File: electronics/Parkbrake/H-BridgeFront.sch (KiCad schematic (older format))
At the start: 74 parts, among them Q19 NX3008CBKS, Q20 IPD031N06L3 G, Q21 IPD031N06L3 G, Q22 IPD031N06L3 G, Q23 IPD031N06L3 G, Q24 NX3008CBKS, Q25 NX3008CBKS, Q26 IPD031N06L3 G, Q27 IPD031N06L3 G, Q28 IPD031N06L3 G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

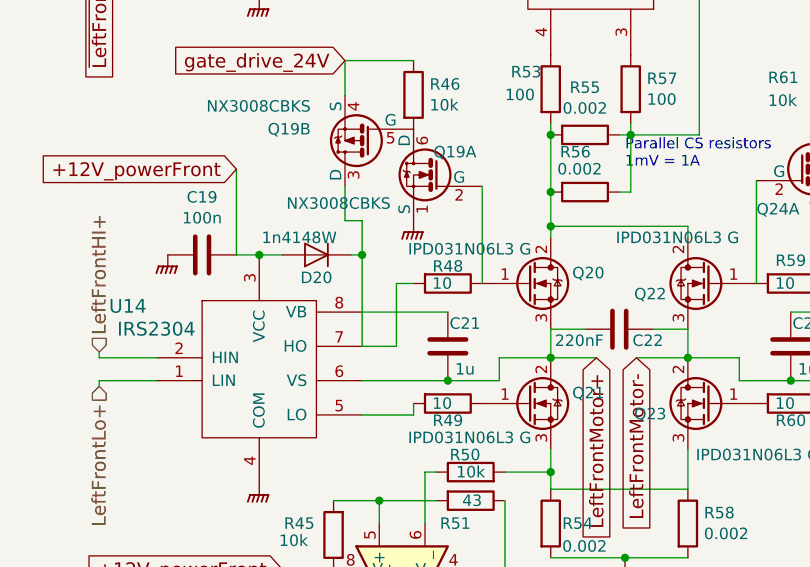
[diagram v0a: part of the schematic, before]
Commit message: Front motors H-bridge finished
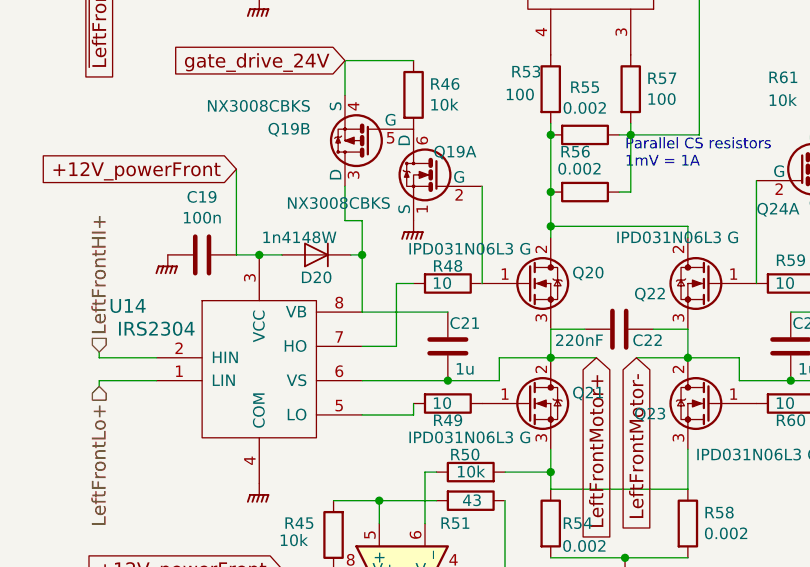
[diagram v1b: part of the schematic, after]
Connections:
- net at D20.1 (K), Q19.3 (D): now also C21.2, U14.8 (VB); no longer R48.2, U14.7 (HO)
- new net: R48.2, U14.7 (HO)
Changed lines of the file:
@@
 $EndComp
 $Comp
-L GNDPWR #PWR42
+L GNDPWR #PWR044
 U 1 1 57012736
 P 3175 4850
-F 0 "#PWR42" H 3175 4650 50  0001 C CNN
+F 0 "#PWR044" H 3175 4650 50  0001 C CNN
 F 1 "GNDPWR" H 3182 4924 50  0001 C CNN
 F 2 "" H 3175 4800 50  0000 C CNN
@@
 $EndComp
 $Comp
-L GNDPWR #PWR46
+L GNDPWR #PWR045
 U 1 1 5797A569
 P 5075 3525
-F 0 "#PWR46" H 5075 3325 50  0001 C CNN
+F 0 "#PWR045" H 5075 3325 50  0001 C CNN
 F 1 "GNDPWR" H 5082 3599 50  0001 C CNN
 F 2 "" H 5075 3475 50  0000 C CNN
@@
 $EndComp
 $Comp
-L GNDPWR #PWR45
+L GNDPWR #PWR046
 U 1 1 57018D81
 P 4675 4525
-F 0 "#PWR45" H 4675 4325 50  0001 C CNN
+F 0 "#PWR046" H 4675 4325 50  0001 C CNN
 F 1 "GNDPWR" H 4682 4599 50  0001 C CNN
 F 2 "" H 4675 4475 50  0000 C CNN
@@
 $EndComp
 $Comp
-L GNDPWR #PWR37
+L GNDPWR #PWR047
 U 1 1 5701B14E
 P 1575 4525
-F 0 "#PWR37" H 1575 4325 50  0001 C CNN
+F 0 "#PWR047" H 1575 4325 50  0001 C CNN
 F 1 "GNDPWR" H 1582 4599 50  0001 C CNN
 F 2 "" H 1575 4475 50  0000 C CNN
@@
 $EndComp
 $Comp
-L GNDPWR #PWR35
+L GNDPWR #PWR048
 U 1 1 5701CA40
 P 1175 3525
-F 0 "#PWR35" H 1175 3325 50  0001 C CNN
+F 0 "#PWR048" H 1175 3325 50  0001 C CNN
 F 1 "GNDPWR" H 1182 3599 50  0001 C CNN
 F 2 "" H 1175 3475 50  0000 C CNN
@@
 $EndComp
 $Comp
-L GNDPWR #PWR38
+L GNDPWR #PWR049
 U 1 1 5701EEBF
 P 1900 5200
-F 0 "#PWR38" H 1900 5000 50  0001 C CNN
+F 0 "#PWR049" H 1900 5000 50  0001 C CNN
 F 1 "GNDPWR" H 1907 5274 50  0001 C CNN
 F 2 "" H 1900 5150 50  0000 C CNN
@@
 $EndComp
 $Comp
-L GNDPWR #PWR41
+L GNDPWR #PWR050
 U 1 1 5701EFC1
 P 2650 4900
-F 0 "#PWR41" H 2650 4700 50  0001 C CNN
+F 0 "#PWR050" H 2650 4700 50  0001 C CNN
 F 1 "GNDPWR" H 2657 4974 50  0001 C CNN
 F 2 "" H 2650 4850 50  0000 C CNN
@@
 $EndComp
 $Comp
-L GNDPWR #PWR54
+L GNDPWR #PWR051
 U 1 1 57031398
 P 8300 4825
-F 0 "#PWR54" H 8300 4625 50  0001 C CNN
+F 0 "#PWR051" H 8300 4625 50  0001 C CNN
 F 1 "GNDPWR" H 8307 4899 50  0001 C CNN
 F 2 "" H 8300 4775 50  0000 C CNN
@@
 $EndComp
 $Comp
-L GNDPWR #PWR58
+L GNDPWR #PWR052
 U 1 1 57031429
 P 10200 3500
-F 0 "#PWR58" H 10200 3300 50  0001 C CNN
+F 0 "#PWR052" H 10200 3300 50  0001 C CNN
 F 1 "GNDPWR" H 10207 3574 50  0001 C CNN
 F 2 "" H 10200 3450 50  0000 C CNN
@@
 $EndComp
 $Comp
-L GNDPWR #PWR57
+L GNDPWR #PWR053
 U 1 1 5703142F
 P 9800 4500
-F 0 "#PWR57" H 9800 4300 50  0001 C CNN
+F 0 "#PWR053" H 9800 4300 50  0001 C CNN
 F 1 "GNDPWR" H 9807 4574 50  0001 C CNN
 F 2 "" H 9800 4450 50  0000 C CNN
@@
 $EndComp
 $Comp
-L GNDPWR #PWR49
+L GNDPWR #PWR054
 U 1 1 5797A59B
 P 6700 4500
-F 0 "#PWR49" H 6700 4300 50  0001 C CNN
+F 0 "#PWR054" H 6700 4300 50  0001 C CNN
 F 1 "GNDPWR" H 6707 4574 50  0001 C CNN
 F 2 "" H 6700 4450 50  0000 C CNN
@@
 $EndComp
 $Comp
-L GNDPWR #PWR47
+L GNDPWR #PWR055
 U 1 1 57031456
 P 6300 3500
-F 0 "#PWR47" H 6300 3300 50  0001 C CNN
+F 0 "#PWR055" H 6300 3300 50  0001 C CNN
 F 1 "GNDPWR" H 6307 3574 50  0001 C CNN
 F 2 "" H 6300 3450 50  0000 C CNN
@@
 $EndComp
 $Comp
-L GNDPWR #PWR50
+L GNDPWR #PWR056
 U 1 1 5703147D
 P 7025 5175
-F 0 "#PWR50" H 7025 4975 50  0001 C CNN
+F 0 "#PWR056" H 7025 4975 50  0001 C CNN
 F 1 "GNDPWR" H 7032 5249 50  0001 C CNN
 F 2 "" H 7025 5125 50  0000 C CNN
@@
 $EndComp
 $Comp
-L GNDPWR #PWR53
+L GNDPWR #PWR057
 U 1 1 5797A5A5
 P 7775 4875
-F 0 "#PWR53" H 7775 4675 50  0001 C CNN
+F 0 "#PWR057" H 7775 4675 50  0001 C CNN
 F 1 "GNDPWR" H 7782 4949 50  0001 C CNN
 F 2 "" H 7775 4825 50  0000 C CNN
@@
 Connection ~ 2400 4075
 Wire Wire Line
-	2400 3775 2025 3775
+	2025 3775 2400 3775
 Wire Wire Line
 	2250 4175 2250 4225
 Wire Wire Line
 	2250 4225 2025 4225
-Wire Wire Line
-	2025 3375 2025 3925
 Wire Wire Line
 	2250 3650 2175 3650
@@
 	1950 2675 1950 2825
 $Comp
-L GNDPWR #PWR44
+L GNDPWR #PWR058
 U 1 1 5797A5B1
 P 4050 3350
-F 0 "#PWR44" H 4050 3150 50  0001 C CNN
+F 0 "#PWR058" H 4050 3150 50  0001 C CNN
 F 1 "GNDPWR" H 4057 3424 50  0001 C CNN
 F 2 "" H 4050 3300 50  0000 C CNN
@@
 $EndComp
 $Comp
-L GNDPWR #PWR39
+L GNDPWR #PWR059
 U 1 1 5704214E
 P 2250 3375
-F 0 "#PWR39" H 2250 3175 50  0001 C CNN
+F 0 "#PWR059" H 2250 3175 50  0001 C CNN
 F 1 "GNDPWR" H 2257 3449 50  0001 C CNN
 F 2 "" H 2250 3325 50  0000 C CNN
@@
 $EndComp
 $Comp
-L GNDPWR #PWR56
+L GNDPWR #PWR060
 U 1 1 5797A5B3
 P 9175 3350
-F 0 "#PWR56" H 9175 3150 50  0001 C CNN
+F 0 "#PWR060" H 9175 3150 50  0001 C CNN
 F 1 "GNDPWR" H 9182 3424 50  0001 C CNN
 F 2 "" H 9175 3300 50  0000 C CNN
@@
 	7675 3625 7675 3200
 $Comp
-L GNDPWR #PWR51
+L GNDPWR #PWR061
 U 1 1 5797A5B6
 P 7375 3350
-F 0 "#PWR51" H 7375 3150 50  0001 C CNN
+F 0 "#PWR061" H 7375 3150 50  0001 C CNN
 F 1 "GNDPWR" H 7382 3424 50  0001 C CNN
 F 2 "" H 7375 3300 50  0000 C CNN
@@
 	7075 2650 7075 2800
 $Comp
-L GNDPWR #PWR36
+L GNDPWR #PWR062
 U 1 1 5797A5B8
 P 1575 2400
-F 0 "#PWR36" H 1575 2200 50  0001 C CNN
+F 0 "#PWR062" H 1575 2200 50  0001 C CNN
 F 1 "GNDPWR" H 1582 2474 50  0001 C CNN
 F 2 "" H 1575 2350 50  0000 C CNN
@@
 $EndComp
 $Comp
-L GNDPWR #PWR48
+L GNDPWR #PWR063
 U 1 1 5797A5B9
 P 6700 2375
-F 0 "#PWR48" H 6700 2175 50  0001 C CNN
+F 0 "#PWR063" H 6700 2175 50  0001 C CNN
 F 1 "GNDPWR" H 6707 2449 50  0001 C CNN
 F 2 "" H 6700 2325 50  0000 C CNN
@@
 	9800 3500 9800 3125
 $Comp
-L GNDPWR #PWR52
+L GNDPWR #PWR064
 U 1 1 579ABEC7
 P 7675 2275
-F 0 "#PWR52" H 7675 2075 50  0001 C CNN
+F 0 "#PWR064" H 7675 2075 50  0001 C CNN
 F 1 "GNDPWR" H 7682 2349 50  0001 C CNN
 F 2 "" H 7675 2225 50  0000 C CNN
@@
 $EndComp
 $Comp
-L GNDPWR #PWR55
+L GNDPWR #PWR065
 U 1 1 579ABFC2
 P 8375 1525
-F 0 "#PWR55" H 8375 1325 50  0001 C CNN
+F 0 "#PWR065" H 8375 1325 50  0001 C CNN
 F 1 "GNDPWR" H 8382 1599 50  0001 C CNN
 F 2 "" H 8375 1475 50  0000 C CNN
@@
 $EndComp
 $Comp
-L GNDPWR #PWR40
+L GNDPWR #PWR066
 U 1 1 579ACE79
 P 2550 2300
-F 0 "#PWR40" H 2550 2100 50  0001 C CNN
+F 0 "#PWR066" H 2550 2100 50  0001 C CNN
 F 1 "GNDPWR" H 2557 2374 50  0001 C CNN
 F 2 "" H 2550 2250 50  0000 C CNN
@@
 $EndComp
 $Comp
-L GNDPWR #PWR43
+L GNDPWR #PWR067
 U 1 1 579AD064
 P 3250 1550
-F 0 "#PWR43" H 3250 1350 50  0001 C CNN
+F 0 "#PWR067" H 3250 1350 50  0001 C CNN
 F 1 "GNDPWR" H 3257 1624 50  0001 C CNN
 F 2 "" H 3250 1500 50  0000 C CNN
@@
 	1    0    0    -1
 $EndComp
+Wire Wire Line
+	2025 3375 2025 3775
 $EndSCHEMATC
